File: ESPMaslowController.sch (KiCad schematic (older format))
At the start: 38 parts, among them J1 Barrel_Jack_Switch, J10 Conn_01x03, J11 Conn_01x03, J2 B6B-PH-SM4-TB, J3 B6B-PH-SM4-TB, J4 B6B-PH-SM4-TB, J5 B6B-PH-SM4-TB, J6 B6B-PH-SM4-TB, J7 Micro_SD_Card_Det, J8 Conn_01x03, J9 Conn_02x12_Odd_Even, U1 NCP3063, U2 ESP32-DevKit-Doit, U3 ATmega328PB-AU

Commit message: Revision v0.1 of PCB fully complete.
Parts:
- C10, C2, C6, C8, C9: LCSC (none) -> C49678; SKU 302010165 -> (none)
- C3: LCSC (none) -> C1728
- C4, C5, C7: LCSC (none) -> C68361
- D1: LCSC (none) -> C28092
- D2, D5: LCSC (none) -> C133102
- D3: LCSC (none) -> C73546
- D4: LCSC (none) -> C72036
- J2, J3, J4, J5, J6: value B6B-PH-SM4-TB -> B6B-PH-K-S; footprint Connector_JST:JST_PH_B6B-PH-SM4-TB_1x06-1MP_P2.00mm_Vertical -> Connector_JST:JST_PH_B6B-PH-K_1x06_P2.00mm_Vertical; MPN B6B-PH-SM4-TB(LF)(SN) -> B6B-PH-K-S(LF)(SN); Price 0.3644 -> 0.33
- L1: LCSC (none) -> C169377; Price (none) -> 1.47
- R1: footprint Resistor_SMD:R_1206_3216Metric -> Resistor_SMD:R_0805_2012Metric; LCSC (none) -> C270926; MFR Yageo -> Ohmite; MPN RL1206FR-070R15L -> KDV08FR150ET; Price 0.36 -> 0.29
- R2, R3, R7, R8: LCSC (none) -> C17414
- R4, R5, R6: LCSC (none) -> C17513
- U1: LCSC (none) -> C41034; MPN NCP3063DR2G -> NCP3063BDR2G; Price 0.89 -> 0.99
- U3: LCSC (none) -> C132230
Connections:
- net AUX1: no longer J9.9 (Pin_9)
- net AUX2: no longer J9.10 (Pin_10)
- net AUX3: no longer J9.13 (Pin_13)
- net AUX4: now also U3.8 (XTAL2/PB7); no longer U3.25 (PC2)
- net AVR_RST: now also U2.21 (GPIO32); no longer U2.11 (GPIO21)
- net DC Driver 1/OUT1: now also J2.2 (Pin_2); no longer J2.1 (Pin_1)
- net DC Driver 1/OUT2: now also J2.1 (Pin_1); no longer J2.2 (Pin_2)
- net DC Driver 2/OUT1: now also J3.2 (Pin_2); no longer J3.1 (Pin_1)
- net DC Driver 2/OUT2: now also J3.1 (Pin_1); no longer J3.2 (Pin_2)
- net DC Driver 3/OUT1: now also J4.2 (Pin_2); no longer J4.1 (Pin_1)
- net DC Driver 3/OUT2: now also J4.1 (Pin_1); no longer J4.2 (Pin_2)
- net DC Driver 4/OUT1: now also J5.2 (Pin_2); no longer J5.1 (Pin_1)
- net DC Driver 4/OUT2: now also J5.1 (Pin_1); no longer J5.2 (Pin_2)
- net DC Driver 5/OUT1: now also J6.2 (Pin_2); no longer J6.1 (Pin_1)
- net DC Driver 5/OUT2: now also J6.1 (Pin_1); no longer J6.2 (Pin_2)
- net DIR1: now also U3.6 (PE1); no longer U3.12 (PB0)
- net DIR2: now also U3.3 (PE0); no longer U3.7 (XTAL1/PB6)
- net DIR3: now also U3.2 (PD4); no longer U3.8 (XTAL2/PB7)
- net DIR4: now also U3.25 (PC2); no longer U3.3 (PE0)
- net DIR5: now also U3.12 (PB0); no longer U3.6 (PE1)
- net ENC3A: now also U2.19 (GPIO34); no longer U2.21 (GPIO32)
- net ENC4A: now also U2.17 (GPIO36); no longer U2.19 (GPIO34)
- net ENC5A: now also U2.14 (GPIO22); no longer U2.17 (GPIO36)
- net ENC5B: now also U2.11 (GPIO21); no longer U2.14 (GPIO22)
- net PWM1: now also U3.31 (PD1); no longer U3.30 (PD0)
- net PWM2: now also U3.32 (PD2); no longer U3.31 (PD1)
- net PWM3: now also U3.1 (PD3); no longer U3.32 (PD2)
- net PWM5: now also U3.30 (PD0); no longer U3.1 (PD3)
- net SD_CLK: now also J9.10 (Pin_10)
- net SD_DI: now also J9.9 (Pin_9)
- net SD_DO: now also J9.13 (Pin_13)

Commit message: Updated LCSC references to match ordered parts.
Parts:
- C3: LCSC C1728 -> C28260
- C4, C5, C7: LCSC C68361 -> C96123
- D1: LCSC C28092 -> (none)
- D2, D5: LCSC C133102 -> (none)
- D3: LCSC C73546 -> C2297
- D4: LCSC C72036 -> C2296
- L1: LCSC C169377 -> (none)
- R1: LCSC C270926 -> (none)
- U1: LCSC C41034 -> (none)
- U3: LCSC C132230 -> (none)
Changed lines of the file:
@@
 F 1 "100n" H 4325 6150 50  0000 L CNN
 F 2 "Capacitor_SMD:C_0805_2012Metric" H 4338 6100 50  0001 C CNN
-F 3 "https://file.elecfans.com/web1/M00/B1/C4/pIYBAF38kjqAET8yABXo2tpxHKE055.pdf?filename=Yageo.pdf" H 4300 6250 50  0001 C CNN
+F 3 "https://www.yageo.com/upload/media/product/productsearch/datasheet/mlcc/UPY-GPHC_X7R_6.3V-to-50V_18.pdf" H 4300 6250 50  0001 C CNN
 F 4 "Yageo" H 4300 6250 50  0001 C CNN "MFR"
 F 5 "CC0805KRX7R9BB104" H 4300 6250 50  0001 C CNN "MPN"
@@
 F 1 "100n" H 4575 3150 50  0000 L CNN
 F 2 "Capacitor_SMD:C_0805_2012Metric" H 4588 3100 50  0001 C CNN
-F 3 "https://file.elecfans.com/web1/M00/B1/C4/pIYBAF38kjqAET8yABXo2tpxHKE055.pdf?filename=Yageo.pdf" H 4550 3250 50  0001 C CNN
+F 3 "https://www.yageo.com/upload/media/product/productsearch/datasheet/mlcc/UPY-GPHC_X7R_6.3V-to-50V_18.pdf" H 4550 3250 50  0001 C CNN
 F 4 "Yageo" H 4550 3250 50  0001 C CNN "MFR"
 F 5 "CC0805KRX7R9BB104" H 4550 3250 50  0001 C CNN "MPN"
@@
 F 1 "100n" H 5775 1000 50  0000 L CNN
 F 2 "Capacitor_SMD:C_0805_2012Metric" H 5788 950 50  0001 C CNN
-F 3 "https://file.elecfans.com/web1/M00/B1/C4/pIYBAF38kjqAET8yABXo2tpxHKE055.pdf?filename=Yageo.pdf" H 5750 1100 50  0001 C CNN
+F 3 "https://www.yageo.com/upload/media/product/productsearch/datasheet/mlcc/UPY-GPHC_X7R_6.3V-to-50V_18.pdf" H 5750 1100 50  0001 C CNN
 F 4 "Yageo" H 5750 1100 50  0001 C CNN "MFR"
 F 5 "CC0805KRX7R9BB104" H 5750 1100 50  0001 C CNN "MPN"
@@
 F 5 "NCP3063BDR2G" H 6700 1300 50  0001 C CNN "MPN"
 F 6 "0.99" H 6700 1300 50  0001 C CNN "Price"
-F 7 "C41034" H 6700 1300 50  0001 C CNN "LCSC"
+F 7 "" H 6700 1300 50  0001 C CNN "LCSC"
 	1    6700 1300
 	1    0    0    -1
@@
 F 5 "CL21B222KBANNNC" H 6050 1150 50  0001 C CNN "MPN"
 F 6 "0.10" H 6050 1150 50  0001 C CNN "Price"
-F 7 "C1728" H 6050 1150 50  0001 C CNN "LCSC"
+F 7 "C28260" H 6050 1150 50  0001 C CNN "LCSC"
 	1    6050 1150
 	1    0    0    -1
@@
 F 5 "KDV08FR150ET" H 7050 650 50  0001 C CNN "MPN"
 F 6 "0.29" H 7050 650 50  0001 C CNN "Price"
-F 7 "C270926" H 7050 650 50  0001 C CNN "LCSC"
+F 7 "" H 7050 650 50  0001 C CNN "LCSC"
 	1    7050 650
 	0    1    1    0
@@
 F 4 "NS12575T680MN" V 8050 1150 50  0001 C CNN "MPN"
 F 5 "Taiyo Yuden" V 8050 1150 50  0001 C CNN "MFR"
-F 6 "C169377" H 8050 1150 50  0001 C CNN "LCSC"
+F 6 "" H 8050 1150 50  0001 C CNN "LCSC"
 F 7 "1.47" H 8050 1150 50  0001 C CNN "Price"
 	1    8050 1150
@@
 F 5 "STPS2L30A" H 7800 1400 50  0001 C CNN "MPN"
 F 6 "0.43" H 7800 1400 50  0001 C CNN "Price"
-F 7 "C133102" H 7800 1400 50  0001 C CNN "LCSC"
+F 7 "" H 7800 1400 50  0001 C CNN "LCSC"
 	1    7800 1400
 	0    1    1    0
@@
 F 5 "CL31A476MQHNNNE" H 8300 1400 50  0001 C CNN "MPN"
 F 6 "0.33" H 8300 1400 50  0001 C CNN "Price"
-F 7 "C68361" H 8300 1400 50  0001 C CNN "LCSC"
+F 7 "C96123" H 8300 1400 50  0001 C CNN "LCSC"
 	1    8300 1400
 	1    0    0    -1
@@
 F 5 "CL31A476MQHNNNE" H 8600 1400 50  0001 C CNN "MPN"
 F 6 "0.33" H 8600 1400 50  0001 C CNN "Price"
-F 7 "C68361" H 8600 1400 50  0001 C CNN "LCSC"
+F 7 "C96123" H 8600 1400 50  0001 C CNN "LCSC"
 	1    8600 1400
 	1    0    0    -1
@@
 F 5 "CL31A476MQHNNNE" H 4250 3250 50  0001 C CNN "MPN"
 F 6 "0.33" H 4250 3250 50  0001 C CNN "Price"
-F 7 "C68361" H 4250 3250 50  0001 C CNN "LCSC"
+F 7 "C96123" H 4250 3250 50  0001 C CNN "LCSC"
 	1    4250 3250
 	1    0    0    -1
@@
 F 5 "STPS2L30A" H 6600 3150 50  0001 C CNN "MPN"
 F 6 "0.43" H 6600 3150 50  0001 C CNN "Price"
-F 7 "C133102" H 6600 3150 50  0001 C CNN "LCSC"
+F 7 "" H 6600 3150 50  0001 C CNN "LCSC"
 	1    6600 3150
 	0    -1   -1   0
@@
 F 5 "LTST-C170KGKT" H 9900 1850 50  0001 C CNN "MPN"
 F 6 "0.35" H 9900 1850 50  0001 C CNN "Price"
-F 7 "C73546" H 9900 1850 50  0001 C CNN "LCSC"
+F 7 "C2297" H 9900 1850 50  0001 C CNN "LCSC"
 	1    9900 1850
 	0    -1   -1   0
@@
 F 5 "LTST-C171KSKT" H 10200 1850 50  0001 C CNN "MPN"
 F 6 "0.31" H 10200 1850 50  0001 C CNN "Price"
-F 7 "C72036" H 10200 1850 50  0001 C CNN "LCSC"
+F 7 "C2296" H 10200 1850 50  0001 C CNN "LCSC"
 	1    10200 1850
 	0    -1   -1   0
@@
 F 5 "ATMEGA328PB-AU" H 9100 4950 50  0001 C CNN "MPN"
 F 6 "1.34" H 9100 4950 50  0001 C CNN "Price"
-F 7 "C132230" H 9100 4950 50  0001 C CNN "LCSC"
+F 7 "" H 9100 4950 50  0001 C CNN "LCSC"
 	1    9100 4950
 	1    0    0    -1
@@
 F 1 "100n" H 8325 3900 50  0000 L CNN
 F 2 "Capacitor_SMD:C_0805_2012Metric" H 8338 3850 50  0001 C CNN
-F 3 "https://file.elecfans.com/web1/M00/B1/C4/pIYBAF38kjqAET8yABXo2tpxHKE055.pdf?filename=Yageo.pdf" H 8300 4000 50  0001 C CNN
+F 3 "https://www.yageo.com/upload/media/product/productsearch/datasheet/mlcc/UPY-GPHC_X7R_6.3V-to-50V_18.pdf" H 8300 4000 50  0001 C CNN
 F 4 "Yageo" H 8300 4000 50  0001 C CNN "MFR"
 F 5 "CC0805KRX7R9BB104" H 8300 4000 50  0001 C CNN "MPN"
@@
 F 1 "100n" H 9475 3050 50  0000 L CNN
 F 2 "Capacitor_SMD:C_0805_2012Metric" H 9488 3000 50  0001 C CNN
-F 3 "https://file.elecfans.com/web1/M00/B1/C4/pIYBAF38kjqAET8yABXo2tpxHKE055.pdf?filename=Yageo.pdf" H 9450 3150 50  0001 C CNN
+F 3 "https://www.yageo.com/upload/media/product/productsearch/datasheet/mlcc/UPY-GPHC_X7R_6.3V-to-50V_18.pdf" H 9450 3150 50  0001 C CNN
 F 4 "Yageo" H 9450 3150 50  0001 C CNN "MFR"
 F 5 "CC0805KRX7R9BB104" H 9450 3150 50  0001 C CNN "MPN"
@@
 F 6 "0.35" H 5150 1100 50  0001 C CNN "Price"
 F 7 "LittelFuse" H 5150 1100 50  0001 C CNN "MFR"
-F 8 "C28092" H 5150 1100 50  0001 C CNN "LCSC"
+F 8 "" H 5150 1100 50  0001 C CNN "LCSC"
 	1    5150 1100
 	0    1    1    0

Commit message: Added some part numbers for the pin headers.
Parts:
- J10, J11, J8: MFR (none) -> Amphenol; MPN (none) -> G800W305018EU; Price (none) -> 0.10
- J9: MFR (none) -> Amphenol; MPN (none) -> G800W590018EU; Price (none) -> 0.23
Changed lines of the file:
@@
 F 1 "Conn_02x12_Odd_Even" H 2650 6550 50  0001 C CNN
 F 2 "Connector_PinHeader_2.54mm:PinHeader_2x12_P2.54mm_Vertical" H 2600 7250 50  0001 C CNN
-F 3 "~" H 2600 7250 50  0001 C CNN
+F 3 "http://www.amphenol-icc.com/media/wysiwyg/files/drawing/g800wxxxxxxeu_2.pdf" H 2600 7250 50  0001 C CNN
+F 4 "Amphenol" H 2600 7250 50  0001 C CNN "MFR"
+F 5 "G800W590018EU" H 2600 7250 50  0001 C CNN "MPN"
+F 6 "0.23" H 2600 7250 50  0001 C CNN "Price"
 	1    2600 7250
 	1    0    0    -1
@@
 F 1 "Conn_01x03" H 1150 6750 50  0001 C CNN
 F 2 "Connector_PinHeader_2.54mm:PinHeader_1x03_P2.54mm_Vertical" H 1150 6950 50  0001 C CNN
-F 3 "~" H 1150 6950 50  0001 C CNN
+F 3 "http://www.amphenol-icc.com/media/wysiwyg/files/drawing/g800wxxxxxxeu_1.pdf" H 1150 6950 50  0001 C CNN
+F 4 "Amphenol" H 1150 6950 50  0001 C CNN "MFR"
+F 5 "G800W305018EU" H 1150 6950 50  0001 C CNN "MPN"
+F 6 "0.10" H 1150 6950 50  0001 C CNN "Price"
 	1    1150 6950
 	1    0    0    -1
@@
 F 1 "Conn_01x03" H 1150 7200 50  0001 C CNN
 F 2 "Connector_PinHeader_2.54mm:PinHeader_1x03_P2.54mm_Vertical" H 1150 7400 50  0001 C CNN
-F 3 "~" H 1150 7400 50  0001 C CNN
+F 3 "http://www.amphenol-icc.com/media/wysiwyg/files/drawing/g800wxxxxxxeu_1.pdf" H 1150 7400 50  0001 C CNN
+F 4 "Amphenol" H 1150 7400 50  0001 C CNN "MFR"
+F 5 "G800W305018EU" H 1150 7400 50  0001 C CNN "MPN"
+F 6 "0.10" H 1150 7400 50  0001 C CNN "Price"
 	1    1150 7400
 	1    0    0    -1
@@
 F 1 "Conn_01x03" H 1150 7650 50  0001 C CNN
 F 2 "Connector_PinHeader_2.54mm:PinHeader_1x03_P2.54mm_Vertical" H 1150 7850 50  0001 C CNN
-F 3 "~" H 1150 7850 50  0001 C CNN
+F 3 "http://www.amphenol-icc.com/media/wysiwyg/files/drawing/g800wxxxxxxeu_1.pdf" H 1150 7850 50  0001 C CNN
+F 4 "Amphenol" H 1150 7850 50  0001 C CNN "MFR"
+F 5 "G800W305018EU" H 1150 7850 50  0001 C CNN "MPN"
+F 6 "0.10" H 1150 7850 50  0001 C CNN "Price"
 	1    1150 7850
 	1    0    0    -1

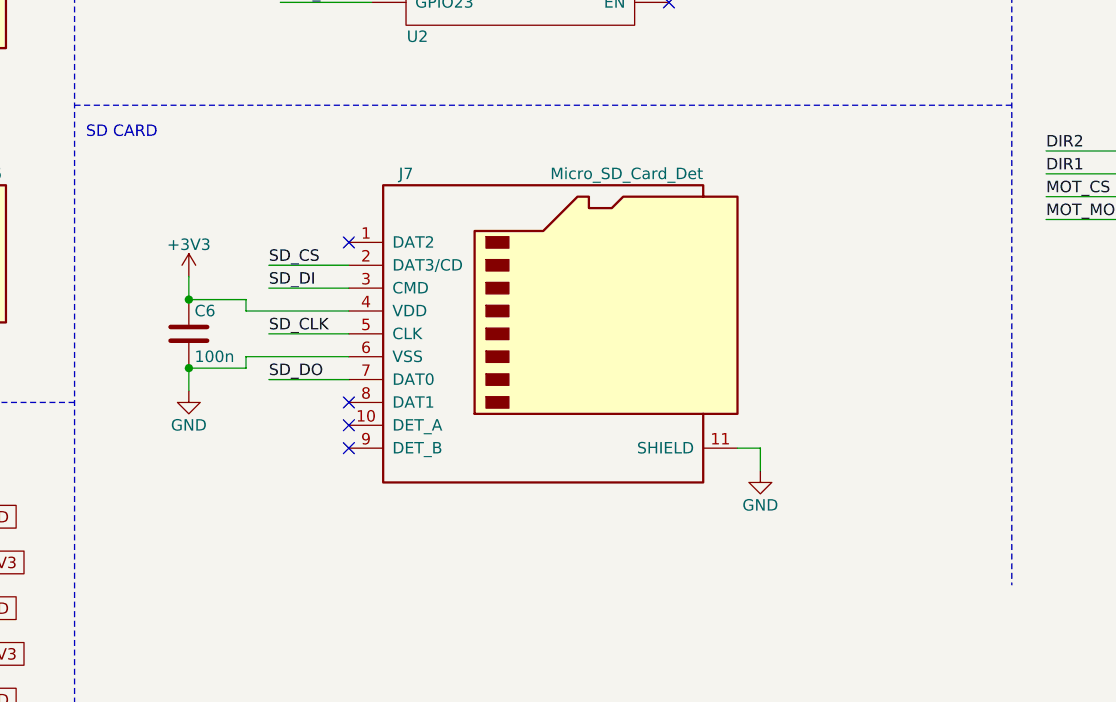
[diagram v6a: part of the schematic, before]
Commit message: Added pullups to unused SD card lines.
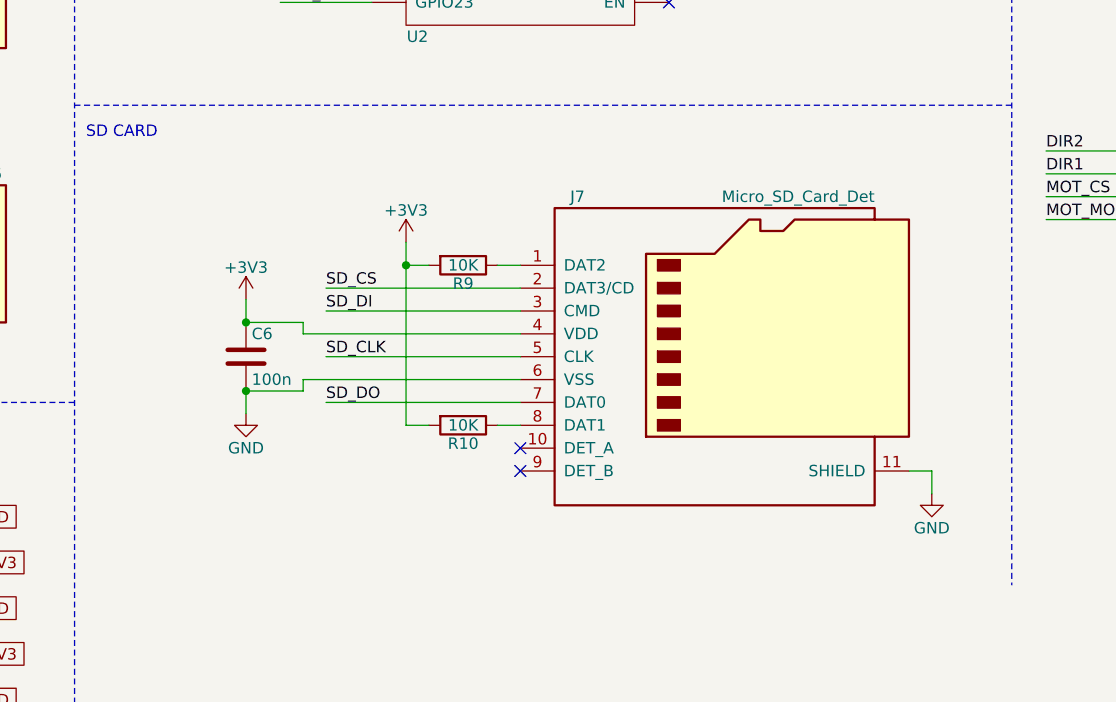
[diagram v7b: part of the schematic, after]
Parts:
- added R10, R9: 10K, Resistor_SMD:R_0805_2012Metric, symbol Device:R
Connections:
- net +3V3: now also R10.2, R9.2
- net at J7.1 (DAT2): now also R9.1
- net at J7.8 (DAT1): now also R10.1
- no-connect marks 12 -> 10
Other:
- moved on the sheet: C6, J7
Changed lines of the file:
@@
 L Connector:Micro_SD_Card_Det J7
 U 1 1 5F6A1474
-P 5900 6250
-F 0 "J7" H 5250 6950 50  0000 C CNN
-F 1 "Micro_SD_Card_Det" H 6550 6950 50  0000 R CNN
-F 2 "Connector_Card:microSD_HC_Hirose_DM3AT-SF-PEJM5" H 7950 6950 50  0001 C CNN
-F 3 "https://www.hirose.com/product/document?clcode=CL0609-0033-6-00&productname=DM3AT-SF-PEJ2M5&series=DM3&documenttype=Catalog&lang=en&documentid=D49662_en" H 5900 6350 50  0001 C CNN
-F 4 "HRS" H 5900 6250 50  0001 C CNN "MFR"
-F 5 "DM3AT-SF-PEJM5" H 5900 6250 50  0001 C CNN "MPN"
-F 6 "2.50" H 5900 6250 50  0001 C CNN "Price"
-	1    5900 6250
+P 6650 6350
+F 0 "J7" H 6000 7050 50  0000 C CNN
+F 1 "Micro_SD_Card_Det" H 7300 7050 50  0000 R CNN
+F 2 "Connector_Card:microSD_HC_Hirose_DM3AT-SF-PEJM5" H 8700 7050 50  0001 C CNN
+F 3 "https://www.hirose.com/product/document?clcode=CL0609-0033-6-00&productname=DM3AT-SF-PEJ2M5&series=DM3&documenttype=Catalog&lang=en&documentid=D49662_en" H 6650 6450 50  0001 C CNN
+F 4 "HRS" H 6650 6350 50  0001 C CNN "MFR"
+F 5 "DM3AT-SF-PEJM5" H 6650 6350 50  0001 C CNN "MPN"
+F 6 "2.50" H 6650 6350 50  0001 C CNN "Price"
+	1    6650 6350
 	1    0    0    -1
 $EndComp
@@
 Wire Wire Line
 	6950 3500 6950 3600
-Text Label 4650 6050 0    50   ~ 0
+Text Label 4900 6150 0    50   ~ 0
 SD_DI
-Text Label 4650 6450 0    50   ~ 0
+Text Label 4900 6550 0    50   ~ 0
 SD_DO
-Text Label 4650 6250 0    50   ~ 0
+Text Label 4900 6350 0    50   ~ 0
 SD_CLK
-Text Label 4650 5950 0    50   ~ 0
+Text Label 4900 6050 0    50   ~ 0
 SD_CS
 Wire Wire Line
-	5000 5950 4650 5950
-Wire Wire Line
-	5000 6050 4650 6050
-Wire Wire Line
-	5000 6250 4650 6250
-Wire Wire Line
-	5000 6450 4650 6450
+	5750 6050 4900 6050
+Wire Wire Line
+	5750 6150 4900 6150
+Wire Wire Line
+	5750 6350 4900 6350
+Wire Wire Line
+	5750 6550 4900 6550
 $Comp
 L power:+3V3 #PWR011
 U 1 1 5F6D002E
-P 4300 6000
-F 0 "#PWR011" H 4300 5850 50  0001 C CNN
-F 1 "+3V3" H 4300 6140 50  0000 C CNN
-F 2 "" H 4300 6000 50  0001 C CNN
-F 3 "" H 4300 6000 50  0001 C CNN
-	1    4300 6000
-	1    0    0    -1
-$EndComp
-Wire Wire Line
-	4300 6000 4300 6100
+P 4550 6100
+F 0 "#PWR011" H 4550 5950 50  0001 C CNN
+F 1 "+3V3" H 4550 6240 50  0000 C CNN
+F 2 "" H 4550 6100 50  0001 C CNN
+F 3 "" H 4550 6100 50  0001 C CNN
+	1    4550 6100
+	1    0    0    -1
+$EndComp
+Wire Wire Line
+	4550 6100 4550 6200
 $Comp
 L power:GND #PWR012
 U 1 1 5F6D1A5F
-P 4300 6500
-F 0 "#PWR012" H 4300 6250 50  0001 C CNN
-F 1 "GND" H 4300 6350 50  0000 C CNN
-F 2 "" H 4300 6500 50  0001 C CNN
-F 3 "" H 4300 6500 50  0001 C CNN
-	1    4300 6500
-	1    0    0    -1
-$EndComp
-Wire Wire Line
-	5000 6350 4550 6350
+P 4550 6600
+F 0 "#PWR012" H 4550 6350 50  0001 C CNN
+F 1 "GND" H 4550 6450 50  0000 C CNN
+F 2 "" H 4550 6600 50  0001 C CNN
+F 3 "" H 4550 6600 50  0001 C CNN
+	1    4550 6600
+	1    0    0    -1
+$EndComp
+Wire Wire Line
+	5750 6450 4800 6450
 $Comp
 L Device:C C6
 U 1 1 5F6D43E4
-P 4300 6250
-F 0 "C6" H 4325 6350 50  0000 L CNN
-F 1 "100n" H 4325 6150 50  0000 L CNN
-F 2 "Capacitor_SMD:C_0805_2012Metric" H 4338 6100 50  0001 C CNN
-F 3 "https://www.yageo.com/upload/media/product/productsearch/datasheet/mlcc/UPY-GPHC_X7R_6.3V-to-50V_18.pdf" H 4300 6250 50  0001 C CNN
-F 4 "Yageo" H 4300 6250 50  0001 C CNN "MFR"
-F 5 "CC0805KRX7R9BB104" H 4300 6250 50  0001 C CNN "MPN"
-F 6 "0.046" H 4300 6250 50  0001 C CNN "Price"
-F 7 "" H 4300 6250 50  0001 C CNN "SKU"
-F 8 "C49678" H 4300 6250 50  0001 C CNN "LCSC"
-	1    4300 6250
-	1    0    0    -1
-$EndComp
-Wire Wire Line
-	4550 6150 4550 6100
-Wire Wire Line
-	4300 6100 4550 6100
-Wire Wire Line
-	4550 6150 5000 6150
-Connection ~ 4300 6100
-Wire Wire Line
-	4550 6350 4550 6400
-Wire Wire Line
-	4550 6400 4300 6400
-Wire Wire Line
-	4300 6400 4300 6500
-Connection ~ 4300 6400
-NoConn ~ 5000 6650
-NoConn ~ 5000 6750
+P 4550 6350
+F 0 "C6" H 4575 6450 50  0000 L CNN
+F 1 "100n" H 4575 6250 50  0000 L CNN
+F 2 "Capacitor_SMD:C_0805_2012Metric" H 4588 6200 50  0001 C CNN
+F 3 "https://www.yageo.com/upload/media/product/productsearch/datasheet/mlcc/UPY-GPHC_X7R_6.3V-to-50V_18.pdf" H 4550 6350 50  0001 C CNN
+F 4 "Yageo" H 4550 6350 50  0001 C CNN "MFR"
+F 5 "CC0805KRX7R9BB104" H 4550 6350 50  0001 C CNN "MPN"
+F 6 "0.046" H 4550 6350 50  0001 C CNN "Price"
+F 7 "" H 4550 6350 50  0001 C CNN "SKU"
+F 8 "C49678" H 4550 6350 50  0001 C CNN "LCSC"
+	1    4550 6350
+	1    0    0    -1
+$EndComp
+Wire Wire Line
+	4800 6250 4800 6200
+Wire Wire Line
+	4550 6200 4800 6200
+Wire Wire Line
+	4800 6250 5750 6250
+Connection ~ 4550 6200
+Wire Wire Line
+	4800 6450 4800 6500
+Wire Wire Line
+	4800 6500 4550 6500
+Wire Wire Line
+	4550 6500 4550 6600
+Connection ~ 4550 6500
+NoConn ~ 5750 6750
+NoConn ~ 5750 6850
 Wire Wire Line
 	4700 3600 5100 3600
@@
 L power:GND #PWR013
 U 1 1 5F816336
-P 6800 6850
-F 0 "#PWR013" H 6800 6600 50  0001 C CNN
-F 1 "GND" H 6800 6700 50  0000 C CNN
-F 2 "" H 6800 6850 50  0001 C CNN
-F 3 "" H 6800 6850 50  0001 C CNN
-	1    6800 6850
-	1    0    0    -1
-$EndComp
-Wire Wire Line
-	6700 6750 6800 6750
-Wire Wire Line
-	6800 6750 6800 6850
+P 7550 6950
+F 0 "#PWR013" H 7550 6700 50  0001 C CNN
+F 1 "GND" H 7550 6800 50  0000 C CNN
+F 2 "" H 7550 6950 50  0001 C CNN
+F 3 "" H 7550 6950 50  0001 C CNN
+	1    7550 6950
+	1    0    0    -1
+$EndComp
+Wire Wire Line
+	7450 6850 7550 6850
+Wire Wire Line
+	7550 6850 7550 6950
 $Comp
 L Device:C C?
@@
 Wire Wire Line
 	9900 800  9900 900
-NoConn ~ 5000 5850
-NoConn ~ 5000 6550
 $Comp
 L MCU_Microchip_ATmega:ATmega328PB-AU U3
@@
 NoConn ~ 9700 5150
 NoConn ~ 9700 6150
+$Comp
+L power:+3V3 #PWR0101
+U 1 1 5F868927
+P 5250 5850
+F 0 "#PWR0101" H 5250 5700 50  0001 C CNN
+F 1 "+3V3" H 5250 5990 50  0000 C CNN
+F 2 "" H 5250 5850 50  0001 C CNN
+F 3 "" H 5250 5850 50  0001 C CNN
+	1    5250 5850
+	1    0    0    -1
+$EndComp
+$Comp
+L Device:R R?
+U 1 1 5F8850B1
+P 5500 5950
+AR Path="/5F746CB5/5F8850B1" Ref="R?"  Part="1"
+AR Path="/5F8850B1" Ref="R9"  Part="1"
+F 0 "R9" V 5580 5950 50  0000 C CNN
+F 1 "10K" V 5500 5950 50  0000 C CNN
+F 2 "Resistor_SMD:R_0805_2012Metric" V 5430 5950 50  0001 C CNN
+F 3 "https://www.yageo.com/upload/media/product/productsearch/datasheet/rchip/PYu-RC_Group_51_RoHS_L_11.pdf" H 5500 5950 50  0001 C CNN
+F 4 "Yageo" H 5500 5950 50  0001 C CNN "MFR"
+F 5 "RC0805FR-0710KL" H 5500 5950 50  0001 C CNN "MPN"
+F 6 "0.10" H 5500 5950 50  0001 C CNN "Price"
+F 7 "C17414" H 5500 5950 50  0001 C CNN "LCSC"
+	1    5500 5950
+	0    1    1    0
+$EndComp
+$Comp
+L Device:R R?
+U 1 1 5F885CFB
+P 5500 6650
+AR Path="/5F746CB5/5F885CFB" Ref="R?"  Part="1"
+AR Path="/5F885CFB" Ref="R10"  Part="1"
+F 0 "R10" V 5580 6650 50  0000 C CNN
+F 1 "10K" V 5500 6650 50  0000 C CNN
+F 2 "Resistor_SMD:R_0805_2012Metric" V 5430 6650 50  0001 C CNN
+F 3 "https://www.yageo.com/upload/media/product/productsearch/datasheet/rchip/PYu-RC_Group_51_RoHS_L_11.pdf" H 5500 6650 50  0001 C CNN
+F 4 "Yageo" H 5500 6650 50  0001 C CNN "MFR"
+F 5 "RC0805FR-0710KL" H 5500 6650 50  0001 C CNN "MPN"
+F 6 "0.10" H 5500 6650 50  0001 C CNN "Price"
+F 7 "C17414" H 5500 6650 50  0001 C CNN "LCSC"
+	1    5500 6650
+	0    1    1    0
+$EndComp
+Wire Wire Line
+	5650 6650 5750 6650
+Wire Wire Line
+	5650 5950 5750 5950
+Wire Wire Line
+	5350 6650 5250 6650
+Wire Wire Line
+	5250 6650 5250 5950
+Wire Wire Line
+	5250 5950 5350 5950
+Wire Wire Line
+	5250 5850 5250 5950
+Connection ~ 5250 5950
 $EndSCHEMATC
